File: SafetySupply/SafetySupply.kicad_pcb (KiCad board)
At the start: 2 copper layers, 30 x 60 mm, 49 parts, among them J1 Screw_Terminal_01x02, J2 Conn_01x01, J3 Screw_Terminal_01x02, J4 Conn_01x01, J5 Screw_Terminal_01x02, J6 Conn_01x01, J7 Conn_01x01, J8 Conn_01x01, J9 Conn_01x01, K1 FRM18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

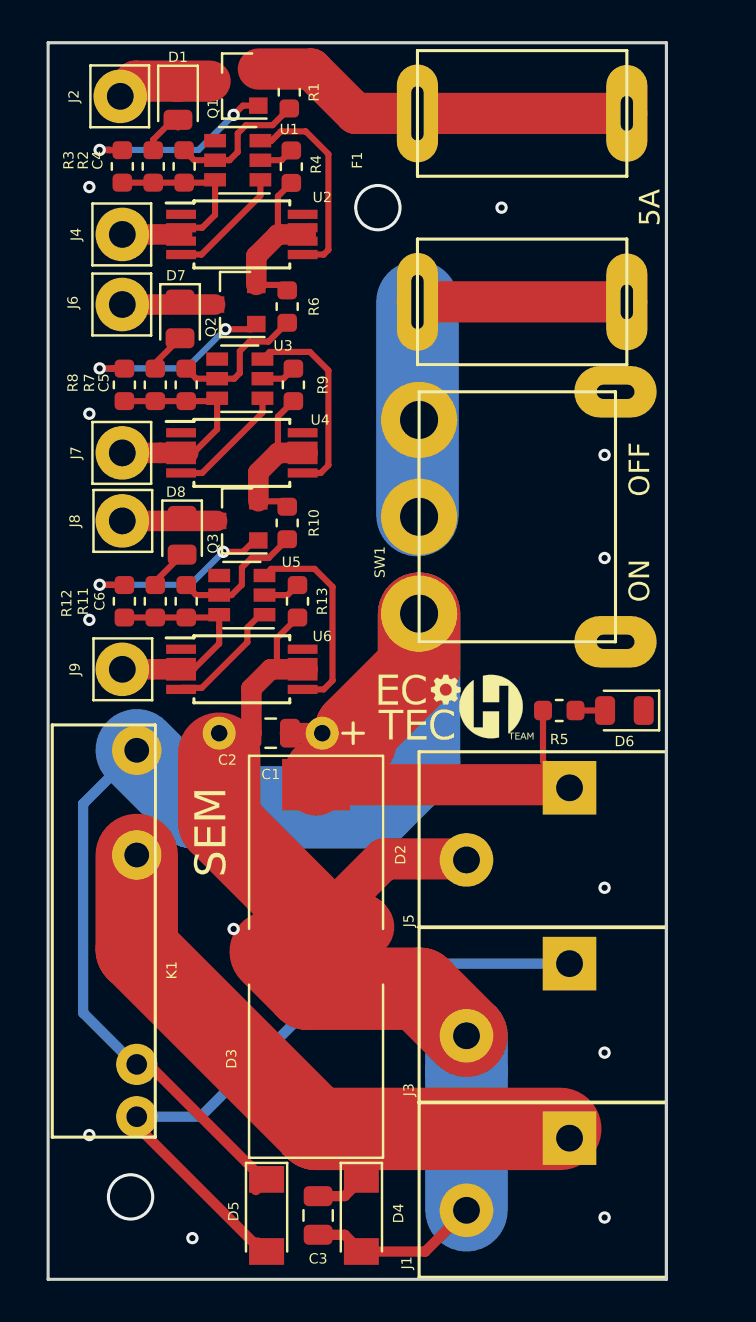
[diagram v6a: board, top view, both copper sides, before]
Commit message: Removed Switches from bus devices and added mounting holes in schematics.
Squashed commit of the following:

commit 448b4f84a5f64686dc4334a0b6d81609891ca7cf
Author: Paweł <mackipawel@gmail.com>
Date:   Sun Apr 28 20:22:14 2019 +0200

    Added mouting holes to SystemSupply.

commit d45917b7024ecbe087cb8328a2c33d3ab10399ff
Author: Paweł <mackipawel@gmail.com>
Date:   Sun Apr 28 20:13:41 2019 +0200

    Added mouting holes to SafetySystem.

commit 6365380671305e2241dc821ec3b00ae08a997ac5
Author: Paweł <mackipawel@gmail.com>
Date:   Sun Apr 28 20:11:13 2019 +0200

    Added mouting holes to SafetySupply.

commit 00163d4bba61eb48f9ebb4c601b04017e78006be
Author: Paweł <mackipawel@gmail.com>
Date:   Sun Apr 28 20:06:38 2019 +0200

    Fixed MotorController.

commit ec0507ca51ef80aebbe2605505e7109beac59e98
Author: Paweł <mackipawel@gmail.com>
Date:   Sun Apr 28 19:54:40 2019 +0200

    Fixed MotorDriver.
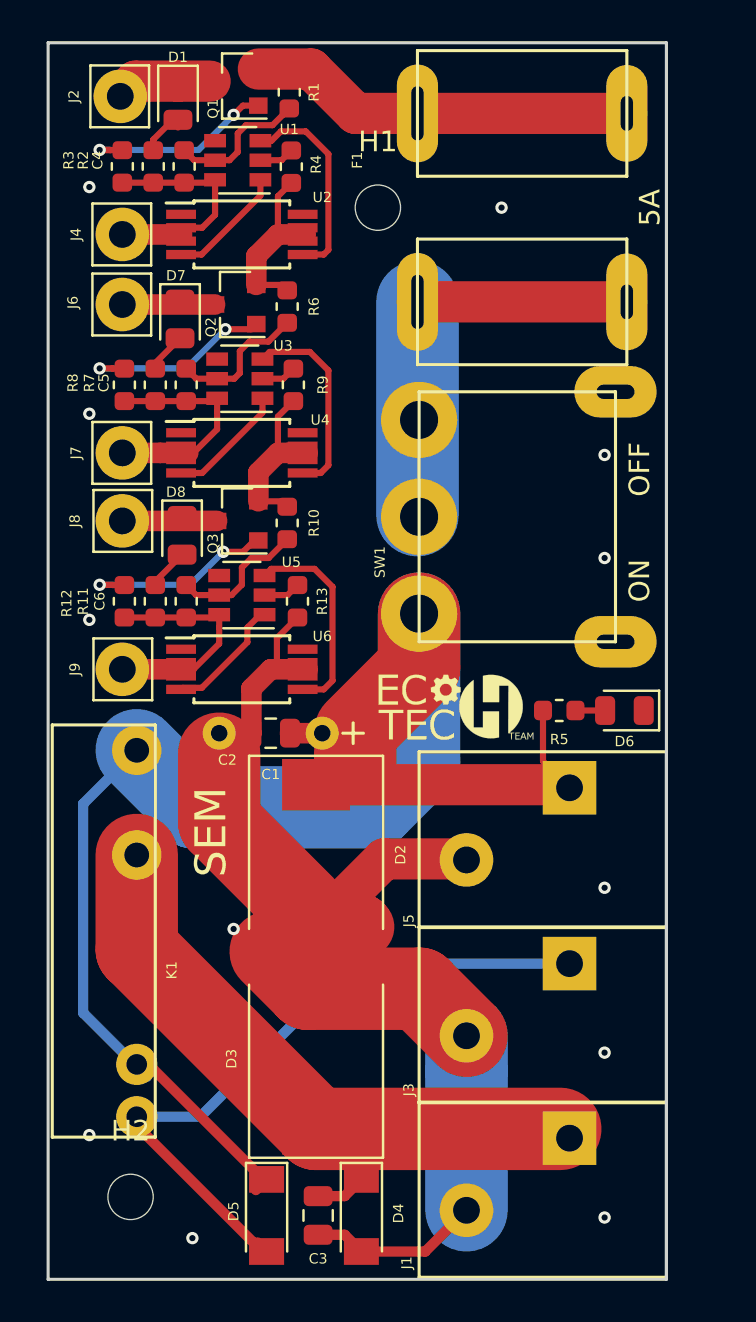
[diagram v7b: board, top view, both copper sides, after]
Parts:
- added H1: MountingHole, MountingHole:MountingHole_2.2mm_M2, F.Cu at (151.0, 69.0)
- added H2: MountingHole, MountingHole:MountingHole_2.2mm_M2, F.Cu at (139.0, 117.0)
- G1: renamed from G***; value LOGO -> EcoTechLogo
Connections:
- SW1 pad 0: GND -> (no net)
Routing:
- net +12V: track 76.4 -> 75.7 mm
- net (no net): vias 2 -> 0
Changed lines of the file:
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@@
     (thickness 1.6)
     (drawings 8)
-    (tracks 233)
+    (tracks 230)
     (zones 0)
-    (modules 49)
+    (modules 51)
     (nets 43)
   )
@@
     (add_net "Net-(U6-Pad8)")
   )
+  (module MountingHole:MountingHole_2.2mm_M2 (layer F.Cu)
+    (at 151 69)
+    (descr "Mounting Hole 2.2mm, no annular, M2")
+    (tags "mounting hole 2.2mm no annular m2")
+    (attr virtual)
+    (fp_text reference H1 (at 0 -3.2) (layer F.SilkS)
+      (effects (font (size 1 1) (thickness 0.15)))
+    )
+    (fp_text value MountingHole (at 0 3.2) (layer F.Fab)
+      (effects (font (size 1 1) (thickness 0.15)))
+    )
+    (fp_circle (center 0 0) (end 2.45 0) (layer F.CrtYd) (width 0.05))
+    (fp_circle (center 0 0) (end 2.2 0) (layer Cmts.User) (width 0.15))
+    (fp_text user %R (at 0.3 0) (layer F.Fab)
+      (effects (font (size 1 1) (thickness 0.15)))
+    )
+    (pad 1 np_thru_hole circle (at 0 0) (size 2.2 2.2) (drill 2.2) (layers *.Cu *.Mask))
+  )
+  (module MountingHole:MountingHole_2.2mm_M2 (layer F.Cu)
+    (at 139 117)
+    (descr "Mounting Hole 2.2mm, no annular, M2")
+    (tags "mounting hole 2.2mm no annular m2")
+    (attr virtual)
+    (fp_text reference H2 (at 0 -3.2) (layer F.SilkS)
+      (effects (font (size 1 1) (thickness 0.15)))
+    )
+    (fp_text value MountingHole (at 0 3.2) (layer F.Fab)
+      (effects (font (size 1 1) (thickness 0.15)))
+    )
+    (fp_text user %R (at 0.3 0) (layer F.Fab)
+      (effects (font (size 1 1) (thickness 0.15)))
+    )
+    (fp_circle (center 0 0) (end 2.2 0) (layer Cmts.User) (width 0.15))
+    (fp_circle (center 0 0) (end 2.45 0) (layer F.CrtYd) (width 0.05))
+    (pad 1 np_thru_hole circle (at 0 0) (size 2.2 2.2) (drill 2.2) (layers *.Cu *.Mask))
+  )
   (module Footprints:C_Radial_D10.0mm_H20.0mm_P5.00mm (layer F.Cu)
     (at 148.3 94.5 180)
@@
     (fp_line (start -6.065 4.53) (end 6.065 4.53) (layer F.SilkS) (width 0.15))
     (fp_line (start -6.065 -5) (end 6.065 -5) (layer F.SilkS) (width 0.15))
-    (pad 0 thru_hole oval (at 6.065 4.53 90) (size 2.5 4) (drill oval 0.7 1.85) (layers *.Cu *.Mask)
-      (net 7 GND))
-    (pad 0 thru_hole oval (at -6.065 4.53 90) (size 2.5 4) (drill oval 0.7 1.85) (layers *.Cu *.Mask)
-      (net 7 GND))
+    (pad 0 thru_hole oval (at 6.065 4.53 90) (size 2.5 4) (drill oval 0.7 1.85) (layers *.Cu *.Mask))
+    (pad 0 thru_hole oval (at -6.065 4.53 90) (size 2.5 4) (drill oval 0.7 1.85) (layers *.Cu *.Mask))
     (pad 3 thru_hole circle (at -4.7 -5 90) (size 3.7 3.7) (drill 1.85) (layers *.Cu *.Mask)
       (net 14 +12V))
@@
   (module Footprints:EcoTech_small (layer F.Cu)
     (at 154.6 93.4)
-    (fp_text reference G*** (at 0 0) (layer F.SilkS) hide
+    (fp_text reference G1 (at 0 0) (layer F.SilkS) hide
       (effects (font (size 1.524 1.524) (thickness 0.3)))
     )
-    (fp_text value LOGO (at 0.75 0) (layer F.SilkS) hide
+    (fp_text value EcoTechLogo (at 0.75 0) (layer F.SilkS) hide
       (effects (font (size 1.524 1.524) (thickness 0.3)))
     )
@@
   (gr_line (start 165 61) (end 135 61) (layer Edge.Cuts) (width 0.15))
   (gr_line (start 165 121) (end 165 61) (layer Edge.Cuts) (width 0.15))
-  (via (at 139 117) (size 2.3) (drill 2) (layers F.Cu B.Cu) (net 0))
-  (via (at 151 69) (size 2.3) (drill 2) (layers F.Cu B.Cu) (net 0))
   (segment (start 141.3 64.7375) (end 141.3 65.1125) (width 0.3) (layer F.Cu) (net 1))
   (segment (start 140.1 65.7) (end 140.1 66.2125) (width 0.3) (layer F.Cu) (net 1))
@@
   (segment (start 160.15 97) (end 160.3 97.15) (width 2) (layer F.Cu) (net 14))
   (segment (start 148.6 97) (end 160.15 97) (width 2) (layer F.Cu) (net 14))
-  (segment (start 148 97) (end 148 96.3) (width 3) (layer F.Cu) (net 14))
-  (segment (start 149.916294 94.400001) (end 149.916294 94.883706) (width 4) (layer F.Cu) (net 14))
-  (segment (start 153 88.7) (end 153 91.316295) (width 4) (layer F.Cu) (net 14))
-  (segment (start 153 91.316295) (end 149.916294 94.400001) (width 4) (layer F.Cu) (net 14))
   (segment (start 145.08 116.67) (end 145.6 116.15) (width 0.5) (layer F.Cu) (net 14))
   (segment (start 136.7 108.07) (end 139.800001 111.170001) (width 0.5) (layer B.Cu) (net 14))
@@
   (segment (start 150.8 98.1) (end 142.07 98.1) (width 4) (layer B.Cu) (net 14))
   (segment (start 142.07 98.1) (end 139.3 95.33) (width 4) (layer B.Cu) (net 14))
+  (segment (start 153 91.316295) (end 149.916294 94.400001) (width 4) (layer F.Cu) (net 14))
+  (segment (start 153 88.7) (end 153 91.316295) (width 4) (layer F.Cu) (net 14))
+  (segment (start 149.9 95.416295) (end 149.9 95.9) (width 4) (layer F.Cu) (net 14))
   (segment (start 140.2 76.5375) (end 141.4 75.3375) (width 0.3) (layer F.Cu) (net 15))
   (segment (start 140.2 76.8125) (end 140.2 76.5375) (width 0.3) (layer F.Cu) (net 15))

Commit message: Added testpoints.
Squashed commit of the following:

commit b78741095f1293168643ce5f943c13a7eb09b318
Author: Paweł <mackipawel@gmail.com>
Date:   Thu May 2 10:22:35 2019 +0200

    Added testpoints to remaining projects.

commit d708f3fd02ddff10684a41533d76b9b66ea6c8f4
Author: Paweł <mackipawel@gmail.com>
Date:   Sun Apr 28 23:49:47 2019 +0200

    Added testpoints in MotorController and MotorDriver.
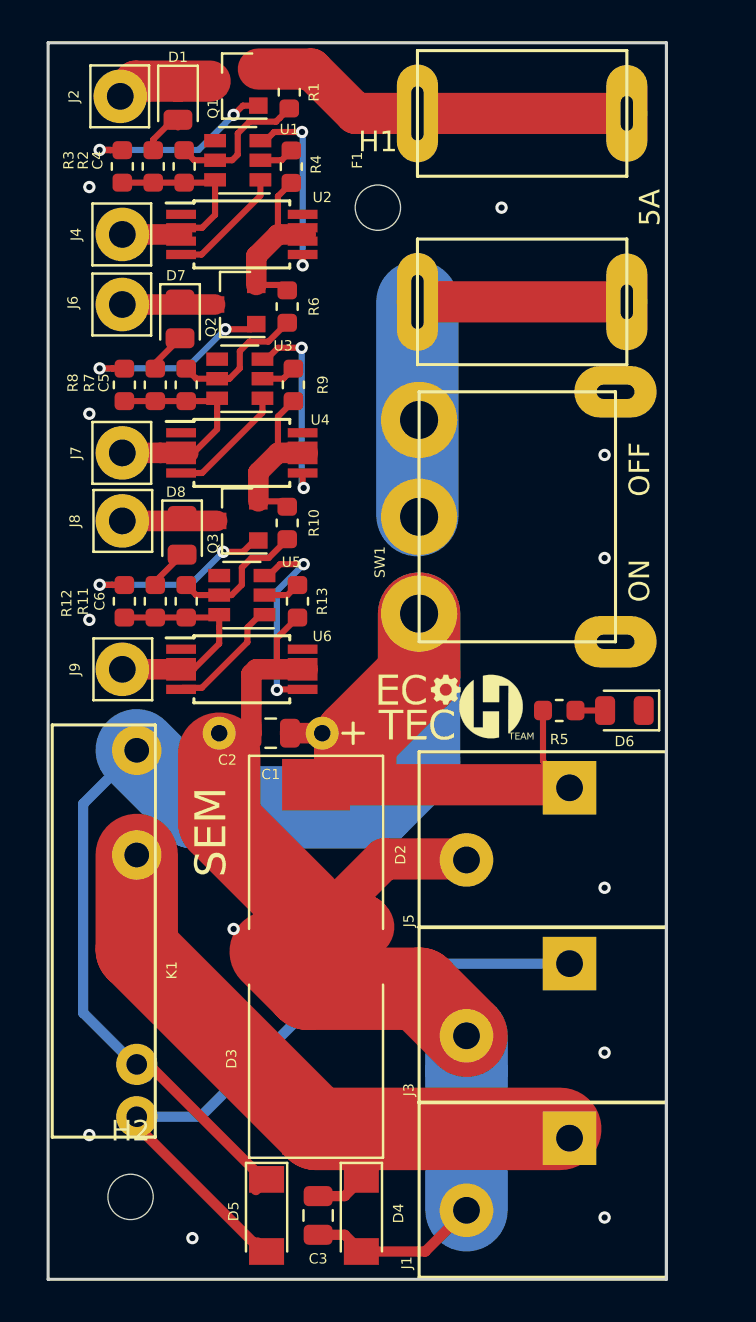
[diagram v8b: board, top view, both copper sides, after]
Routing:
- net +12V: track 75.7 -> 76.7 mm
- net Net-(U1-Pad3): track 9.94 -> 9.20 mm, vias 0 -> 2
- net Net-(U5-Pad3): track 9.97 -> 10.0 mm, vias 0 -> 2
- net Net-(U3-Pad3): track 9.72 -> 9.71 mm, vias 0 -> 2
